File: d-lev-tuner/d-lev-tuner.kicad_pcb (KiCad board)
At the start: 4 copper layers, 88.7 x 68.4 mm, 38 parts, among them J1 S6B-PH-SM4-TB, U1 STP08CP05, U2 STP08CP05, U3 AP2112K-3.3, U4 STP08CP05, U5 DSM7TA56

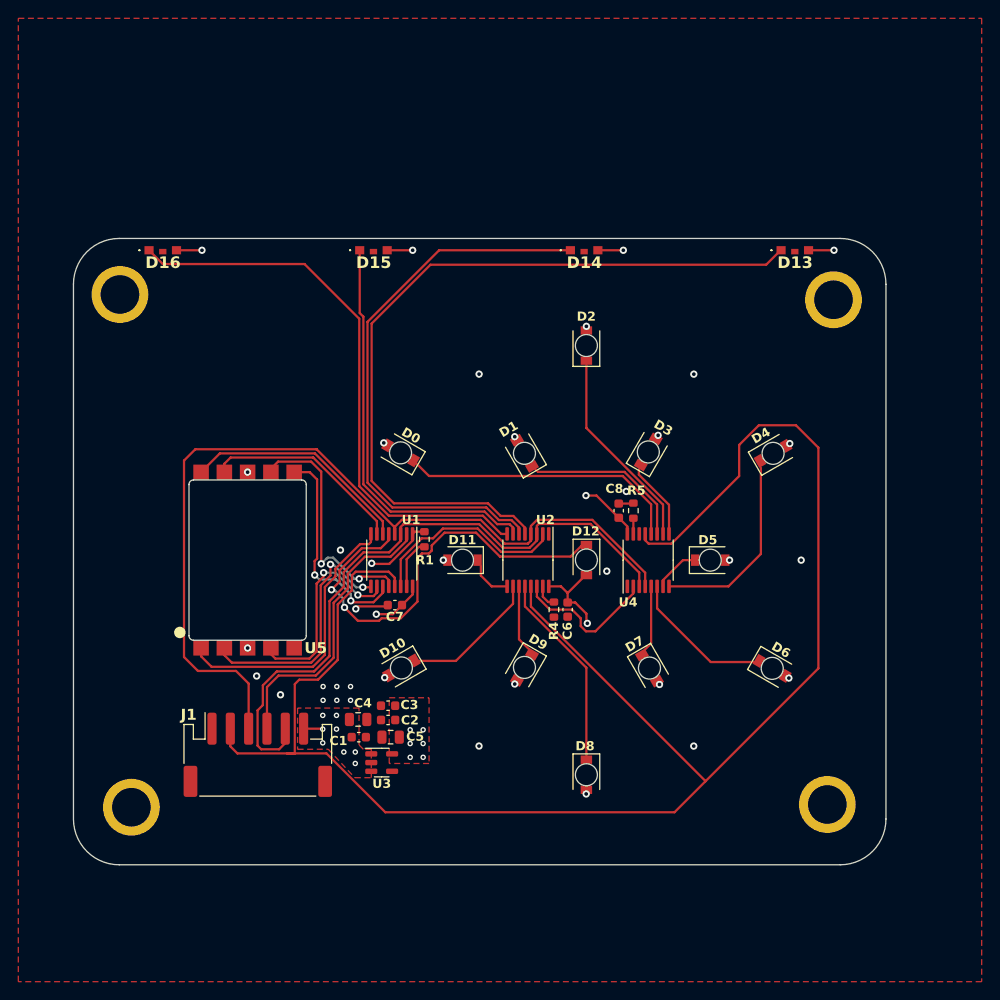
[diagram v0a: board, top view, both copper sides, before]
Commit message: tuner: fixed led footprints
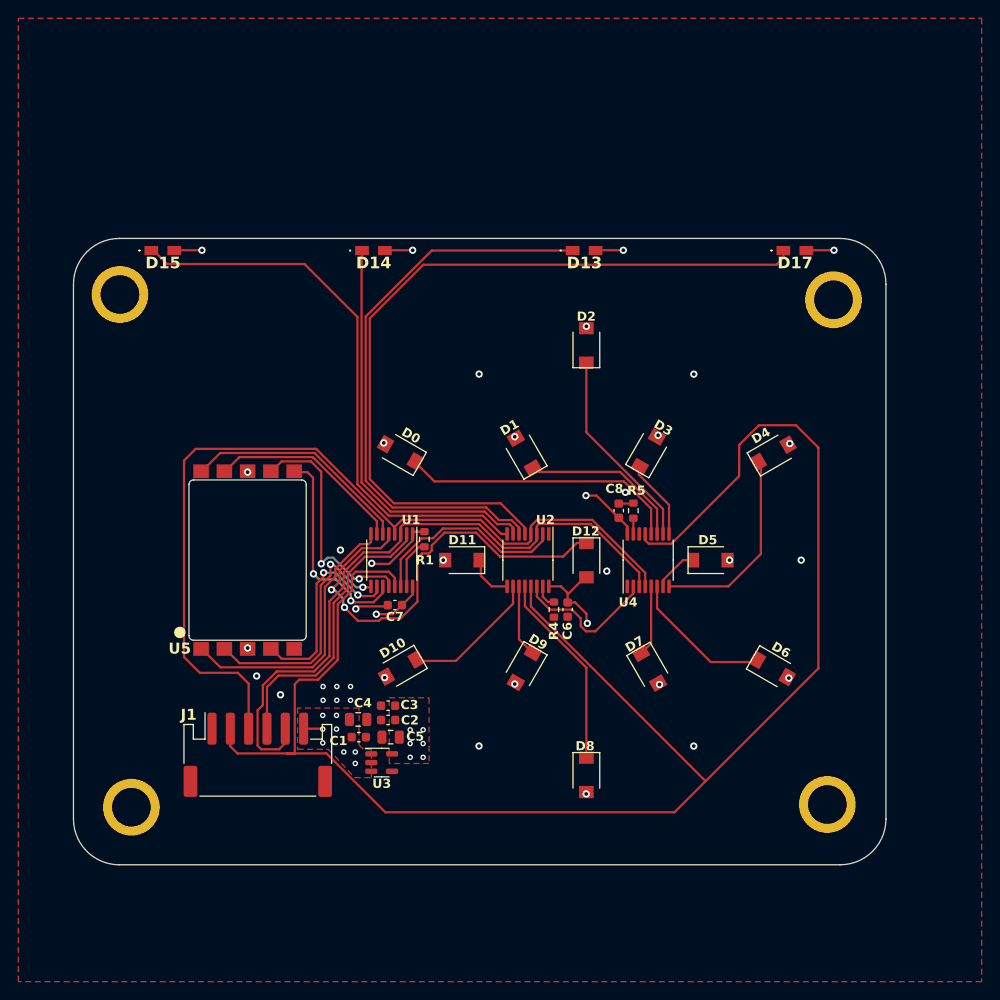
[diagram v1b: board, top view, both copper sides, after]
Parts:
- removed D16: LED_Pad, d-lev:S220TBKT
- added D17: LTST-S220TBKT, d-lev:S220TBKT, F.Cu at (122.9, 32.6)
- D0, D1, D10, D11, D12, D2, D3, D4, D5, D6, D7, D8, D9: value LED -> LTST-C250TBKT
- D13, D14, D15: value LED_Pad -> LTST-S220TBKT
- H1, H2, H3, H4: value MountingHole_Pad -> SMTSO-M3-2ET
- moved D15 23.0 mm to (53.9, 32.6)
- moved D13 23.0 mm to (99.9, 32.6)
- moved D14 23.0 mm to (76.9, 32.6)
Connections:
- D13 pad 1: LED13 -> LED14
- D14 pad 1: LED14 -> LED15
- D15 pad 1: LED15 -> LED16
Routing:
- net LED13: track 84.7 -> 86.1 mm
- net LED14: track 62.2 -> 63.1 mm
- net F: track 22.1 -> 21.6 mm

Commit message: star pattern done
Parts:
- added REF**: star-pattern, art:star-pattern, B.Cu at (100.2, 66.4)
- moved D7 0.19 mm to (106.9, 78.1)
- moved D6 0.16 mm to (120.4, 78.1)
- moved D4 0.14 mm to (120.4, 54.7)
- moved D3 0.12 mm to (106.9, 54.7)
- moved D10 0.09 mm to (79.9, 78.1)
- moved D0 0.07 mm to (79.9, 54.7)
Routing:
- net LED12: track 48.4 -> 50.5 mm
- net /Net-(U3-SDI): track 22.1 -> 24.0 mm
- net CLK: track 72.4 -> 74.1 mm
- net LE: track 97.8 -> 99.6 mm
- net LED4: track 20.9 -> 22.0 mm
- net LED6: track 15.3 -> 14.5 mm
- net LED16: track 62.4 -> 63.1 mm
- net LED11: track 4.41 -> 5.01 mm
- net LED9: track 7.24 -> 7.82 mm
- net LED7: track 7.13 -> 7.69 mm
- added copper zone on B.Cu, net GND

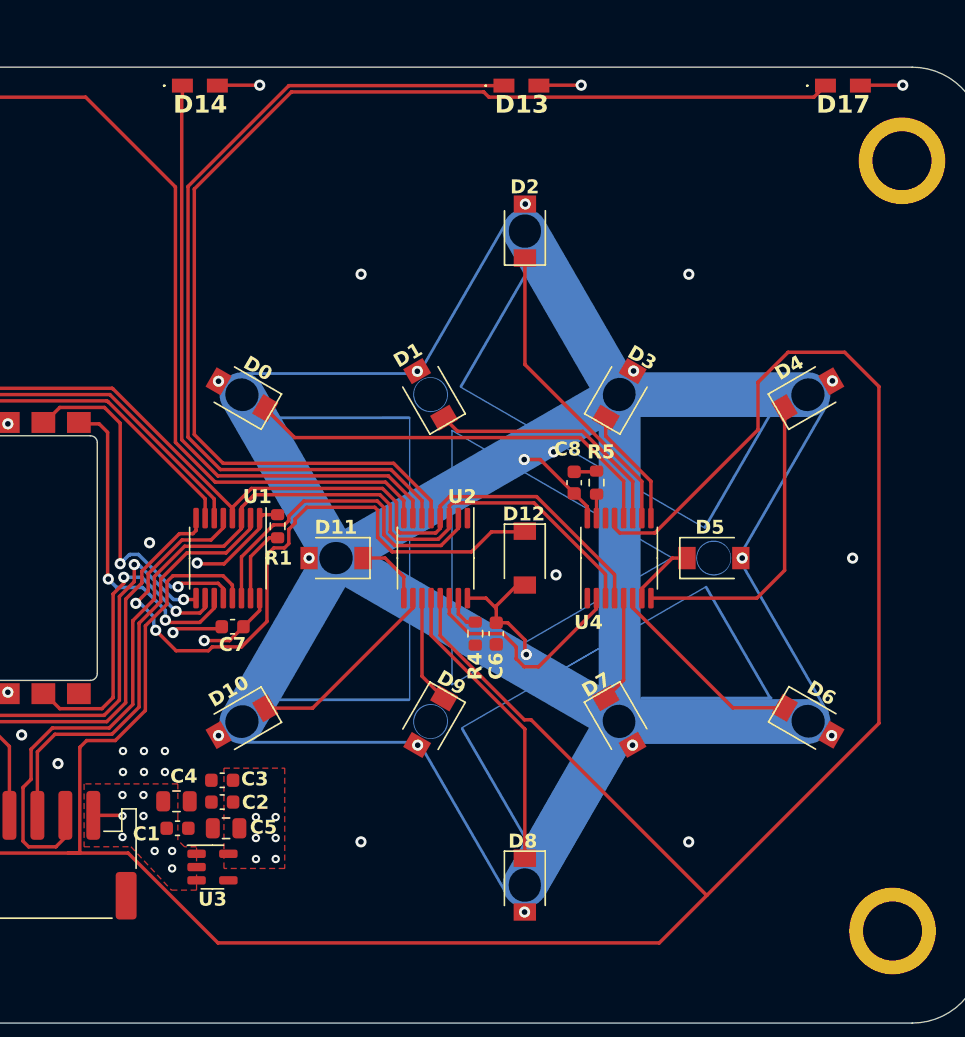
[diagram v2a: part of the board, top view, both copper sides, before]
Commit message: tuner: pass drc
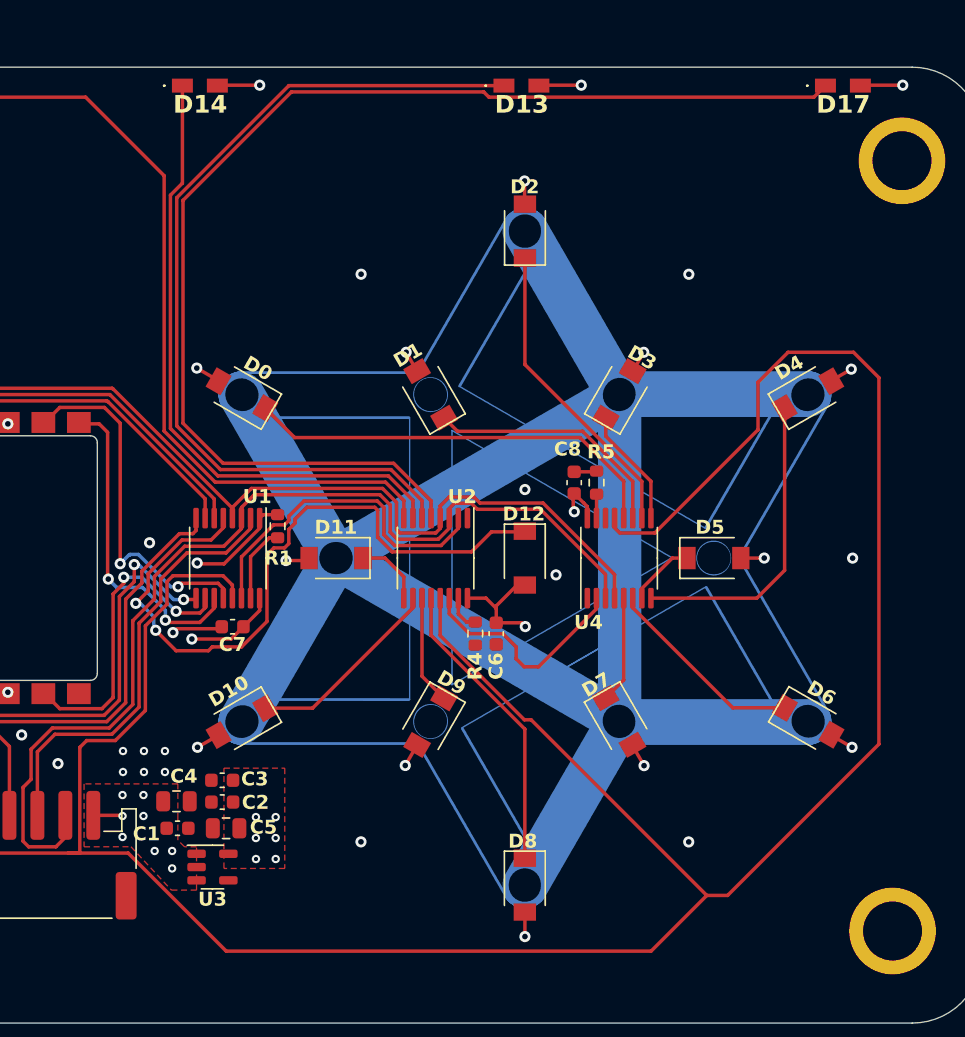
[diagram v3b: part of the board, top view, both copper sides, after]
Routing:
- net +3V3: track 33.5 -> 49.8 mm
- net OE: track 187.4 -> 189.1 mm
- net LED15: track 45.0 -> 45.6 mm
- net LED14: track 63.4 -> 64.1 mm
- net LED13: track 86.2 -> 86.9 mm

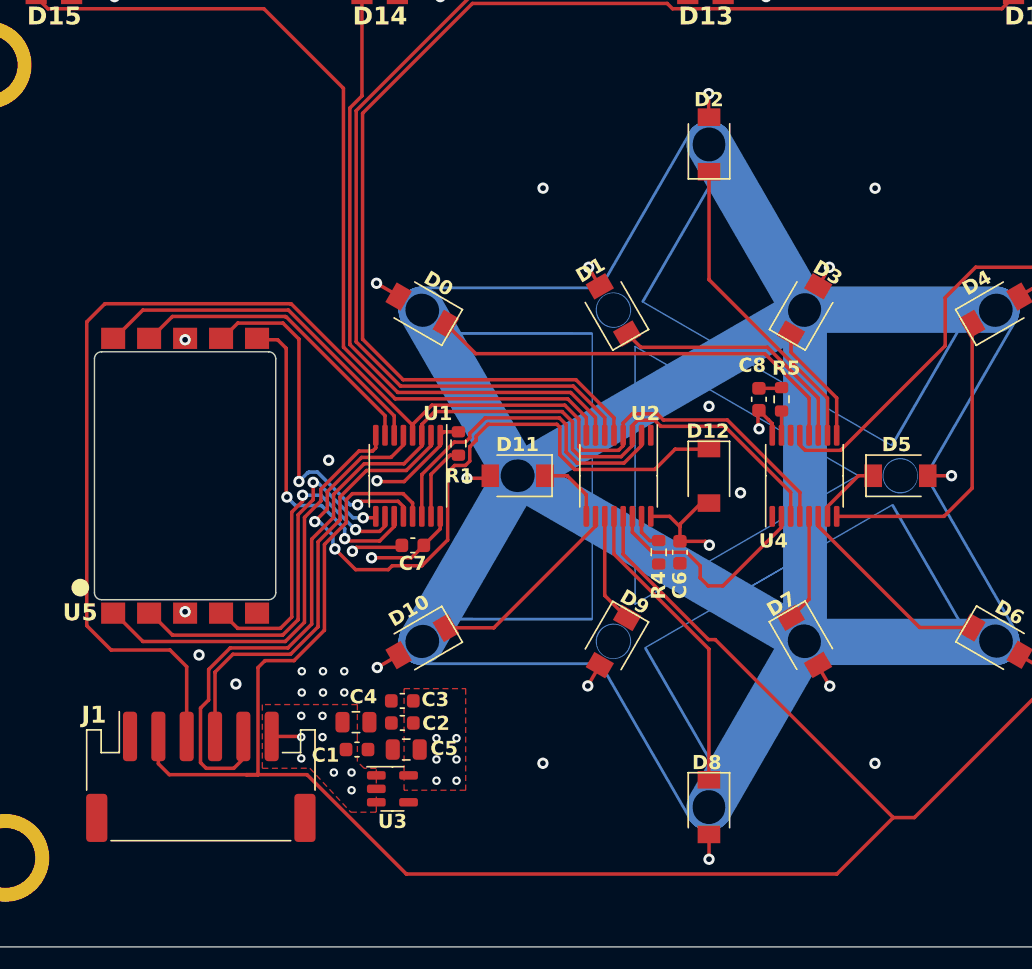
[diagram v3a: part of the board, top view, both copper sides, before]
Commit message: everything passes drc as much as i care for it to, added silk art
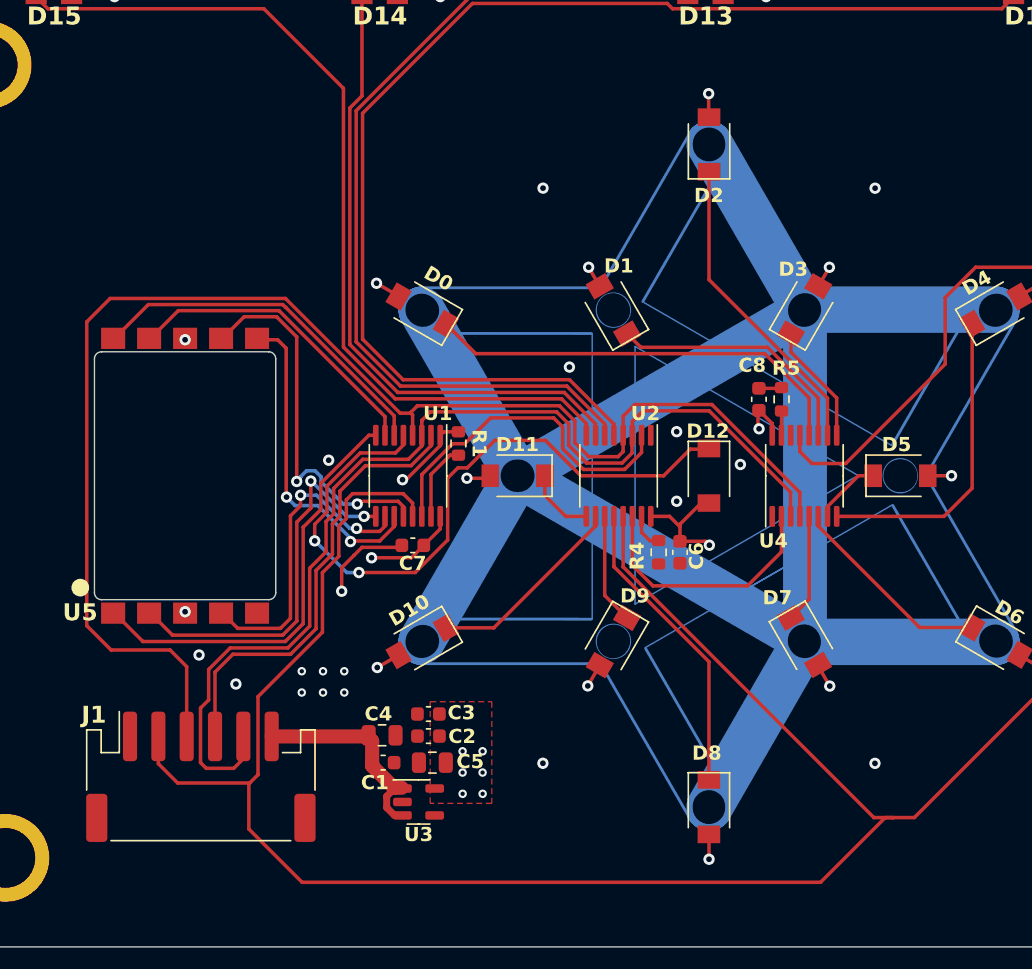
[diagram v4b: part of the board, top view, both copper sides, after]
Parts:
- added G***: LOGO, LOGO, F.Cu at (63.4, 44.8)
- moved C5 2.06 mm to (80.6, 86.7)
- moved C1 2.06 mm to (77.1, 86.7)
- moved C2 2.06 mm to (80.3, 84.8)
- moved C3 2.06 mm to (80.3, 83.2)
- moved C4 2.06 mm to (77.1, 84.7)
- moved U3 2.06 mm to (79.6, 89.4)
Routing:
- net +5V: track 2.11 -> 15.3 mm, vias 8 -> 0
- net OE: track 189.1 -> 192.7 mm
- net LED12: track 50.5 -> 48.5 mm
- net Net-(U2-SDO): track 16.2 -> 18.1 mm
- net LE: track 99.5 -> 101.2 mm
- net GND: track 12.9 -> 13.7 mm, vias 18 -> 20
- net A: track 26.1 -> 26.8 mm
- net +3V3: track 49.8 -> 49.2 mm
- removed copper zone on F.Cu, net +5V

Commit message: Add JLC releases
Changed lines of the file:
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@@
     (fp_circle (center -20.25 11.691343) (end -19.05 11.691343)
-      (stroke (width 0.1) (type default)) (fill none) (layer "B.Cu"))
-    (fp_circle (center -13.5 0) (end -12.3 0)
       (stroke (width 0.1) (type default)) (fill none) (layer "B.Cu"))
     (fp_circle (center -6.75 -11.691343) (end -5.55 -11.691343)
@@
       (stroke (width 0.1) (type default)) (fill none) (layer "B.Cu"))
     (fp_circle (center 0 23.382686) (end 1.2 23.382686)
-      (stroke (width 0.1) (type default)) (fill none) (layer "B.Cu"))
-    (fp_circle (center 6.75 -11.691343) (end 7.95 -11.691343)
-      (stroke (width 0.1) (type default)) (fill none) (layer "B.Cu"))
-    (fp_circle (center 6.75 11.691343) (end 7.95 11.691343)
       (stroke (width 0.1) (type default)) (fill none) (layer "B.Cu"))
     (fp_circle (center 13.5 0) (end 14.7 0)
@@
     (fp_poly
       (pts
+        (xy 6.72978 11.729267)
+        (xy -13.52022 0.037924)
+        (xy 6.72978 -11.653419)
+      )
+      (stroke (width 3.1) (type solid)) (fill none) (layer "B.Mask"))
+    (fp_poly
+      (pts
         (xy 13.474815 0.009488)
         (xy -6.775185 11.700831)
@@
     (fp_poly
       (pts
-        (xy 5.219999 -12.5)
-        (xy 5.220007 12.58)
-        (xy 8.245296 13.166614)
-        (xy 8.248279 -13.236672)
-      )
-      (stroke (width 0.1) (type solid)) (fill solid) (layer "B.Mask"))
-    (fp_poly
-      (pts
-        (xy 7.231587 13.754871)
-        (xy -15.448317 0.660376)
-        (xy -12.652724 -1.213473)
-        (xy 8.25 10.88)
-      )
-      (stroke (width 0.1) (type solid)) (fill solid) (layer "B.Mask"))
-    (fp_poly
-      (pts
-        (xy 7.29 -13.74)
-        (xy -15.581607 -0.53674)
-        (xy -12.79 1.33)
-        (xy 8.06787 -10.701913)
-      )
-      (stroke (width 0.1) (type solid)) (fill solid) (layer "B.Mask"))
-    (fp_poly
-      (pts

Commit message: Add iBOMs and additional part numbers
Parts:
- C2, C6, C7, C8: value .1u -> 100n
